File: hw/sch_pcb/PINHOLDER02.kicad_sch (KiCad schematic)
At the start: 5 parts, among them J1 HEADER_1x03, M3 HOLE, M4 HOLE

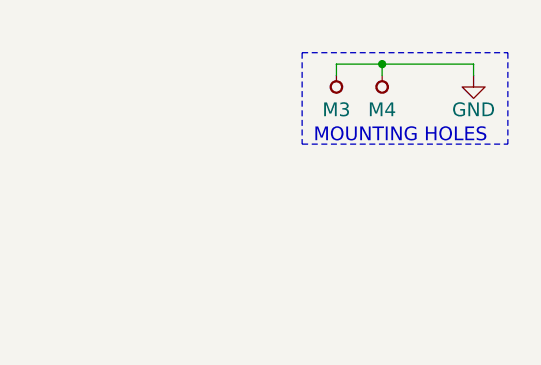
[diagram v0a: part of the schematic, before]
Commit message: uprava layoutu pro PCRD01A
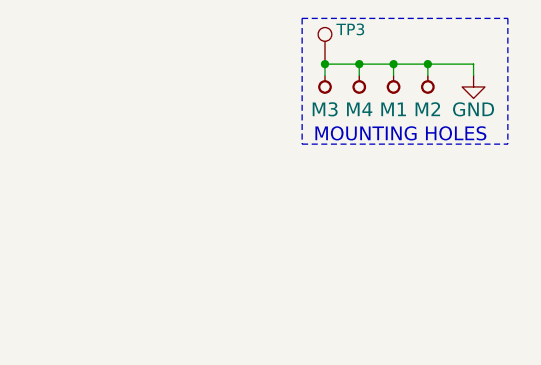
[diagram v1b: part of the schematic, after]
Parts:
- added M1, M2: HOLE, Mlab_Mechanical:MountingHole_3mm, symbol MLAB_MECHANICAL:HOLE
- added TP3: TestPoint, Mlab_CON:TestPoint_Pad_D0.5mm_noSilk, symbol Connector:TestPoint
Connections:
- net GND: now also M1.1, M2.1, TP3.1
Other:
- title: PINHOLDER01A -> PINHOLDER02A
- moved on the sheet: M3, M4
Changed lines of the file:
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@@
   (paper "A4")
   (title_block
-    (title "PINHOLDER01A")
+    (title "PINHOLDER02A")
     (date "2023-04-12")
-    (rev "01A")
+    (rev "02A")
     (company "www.mlab.cz")
   )
-  (junction (at 262.89 22.86) (diameter 0) (color 0 0 0 0)
-  )
-  (wire (pts (xy 262.89 24.13) (xy 262.89 22.86))
+  (junction (at 264.16 22.86) (diameter 0) (color 0 0 0 0)
+  )
+  (junction (at 267.97 22.86) (diameter 0) (color 0 0 0 0)
+  )
+  (junction (at 260.35 22.86) (diameter 0) (color 0 0 0 0)
+  )
+  (junction (at 256.54 22.86) (diameter 0) (color 0 0 0 0)
+  )
+  (wire (pts (xy 267.97 22.86) (xy 267.97 24.13))
+    (stroke (width 0) (type default) (color 0 0 0 0))
+  )
+  (wire (pts (xy 260.35 24.13) (xy 260.35 22.86))
+    (stroke (width 0) (type solid) (color 0 0 0 0))
+  )
+  (wire (pts (xy 260.35 22.86) (xy 264.16 22.86))
     (stroke (width 0) (type solid) (color 0 0 0 0))
   )
@@
     (stroke (width 0) (type default) (color 0 0 0 0))
   )
-  (wire (pts (xy 262.89 22.86) (xy 273.05 22.86))
-    (stroke (width 0) (type solid) (color 0 0 0 0))
-  )
   (wire (pts (xy 116.84 101.6) (xy 146.05 101.6))
     (stroke (width 0) (type default) (color 0 0 0 0))
@@
     (stroke (width 0) (type dash) (color 0 0 0 0))
   )
-  (polyline (pts (xy 254 21.59) (xy 276.86 21.59))
+  (polyline (pts (xy 254 17.78) (xy 276.86 17.78))
     (stroke (width 0) (type dash) (color 0 0 0 0))
   )
@@
     (stroke (width 0) (type default) (color 0 0 0 0))
   )
-  (polyline (pts (xy 276.86 21.59) (xy 276.86 31.75))
+  (polyline (pts (xy 276.86 17.78) (xy 276.86 31.75))
     (stroke (width 0) (type dash) (color 0 0 0 0))
   )
@@
     (stroke (width 0) (type default) (color 0 0 0 0))
   )
-  (wire (pts (xy 257.81 24.13) (xy 257.81 22.86))
-    (stroke (width 0) (type solid) (color 0 0 0 0))
-  )
-  (wire (pts (xy 257.81 22.86) (xy 262.89 22.86))
-    (stroke (width 0) (type solid) (color 0 0 0 0))
-  )
-  (polyline (pts (xy 254 21.59) (xy 254 31.75))
-    (stroke (width 0) (type dash) (color 0 0 0 0))
+  (wire (pts (xy 264.16 22.86) (xy 264.16 24.13))
+    (stroke (width 0) (type default) (color 0 0 0 0))
+  )
+  (wire (pts (xy 264.16 22.86) (xy 267.97 22.86))
+    (stroke (width 0) (type solid) (color 0 0 0 0))
+  )
+  (wire (pts (xy 256.54 24.13) (xy 256.54 22.86))
+    (stroke (width 0) (type solid) (color 0 0 0 0))
+  )
+  (wire (pts (xy 256.54 22.86) (xy 260.35 22.86))
+    (stroke (width 0) (type solid) (color 0 0 0 0))
+  )
+  (polyline (pts (xy 254 17.78) (xy 254 31.75))
+    (stroke (width 0) (type dash) (color 0 0 0 0))
+  )
+  (wire (pts (xy 267.97 22.86) (xy 273.05 22.86))
+    (stroke (width 0) (type solid) (color 0 0 0 0))
   )
   (text "MOUNTING HOLES" (at 255.27 31.75 0)
@@
     (pin "1")
   )
-  (symbol (lib_id "MLAB_MECHANICAL:HOLE") (at 257.81 25.4 90) (unit 1)
-    (in_bom yes) (on_board yes)
-    (property "Reference" "M3" (id 0) (at 257.81 27.94 90)
-      (effects (font (size 1.524 1.524)))
-    )
-    (property "Value" "HOLE" (id 1) (at 260.35 25.4 0)
-      (effects (font (size 1.524 1.524)) hide)
-    )
-    (property "Footprint" "Mlab_Mechanical:MountingHole_3mm" (id 2) (at 257.81 25.4 0)
-      (effects (font (size 1.524 1.524)) hide)
-    )
-    (property "Datasheet" "" (id 3) (at 257.81 25.4 0)
-      (effects (font (size 1.524 1.524)))
+  (symbol (lib_id "MLAB_MECHANICAL:HOLE") (at 264.16 25.4 90) (unit 1)
+    (in_bom yes) (on_board yes)
+    (property "Reference" "M1" (id 0) (at 264.16 27.94 90)
+      (effects (font (size 1.524 1.524)))
+    )
+    (property "Value" "HOLE" (id 1) (at 266.7 25.4 0)
+      (effects (font (size 1.524 1.524)) hide)
+    )
+    (property "Footprint" "Mlab_Mechanical:MountingHole_3mm" (id 2) (at 264.16 25.4 0)
+      (effects (font (size 1.524 1.524)) hide)
+    )
+    (property "Datasheet" "" (id 3) (at 264.16 25.4 0)
+      (effects (font (size 1.524 1.524)))
+    )
+    (pin "1")
+  )
+  (symbol (lib_id "MLAB_MECHANICAL:HOLE") (at 256.54 25.4 90) (unit 1)
+    (in_bom yes) (on_board yes)
+    (property "Reference" "M3" (id 0) (at 256.54 27.94 90)
+      (effects (font (size 1.524 1.524)))
+    )
+    (property "Value" "HOLE" (id 1) (at 259.08 25.4 0)
+      (effects (font (size 1.524 1.524)) hide)
+    )
+    (property "Footprint" "Mlab_Mechanical:MountingHole_3mm" (id 2) (at 256.54 25.4 0)
+      (effects (font (size 1.524 1.524)) hide)
+    )
+    (property "Datasheet" "" (id 3) (at 256.54 25.4 0)
+      (effects (font (size 1.524 1.524)))
+    )
+    (pin "1")
+  )
+  (symbol (lib_id "MLAB_MECHANICAL:HOLE") (at 267.97 25.4 90) (unit 1)
+    (in_bom yes) (on_board yes)
+    (property "Reference" "M2" (id 0) (at 267.97 27.94 90)
+      (effects (font (size 1.524 1.524)))
+    )
+    (property "Value" "HOLE" (id 1) (at 270.51 25.4 0)
+      (effects (font (size 1.524 1.524)) hide)
+    )
+    (property "Footprint" "Mlab_Mechanical:MountingHole_3mm" (id 2) (at 267.97 25.4 0)
+      (effects (font (size 1.524 1.524)) hide)
+    )
+    (property "Datasheet" "" (id 3) (at 267.97 25.4 0)
+      (effects (font (size 1.524 1.524)))
+    )
+    (pin "1")
+  )
+  (symbol (lib_id "Connector:TestPoint") (at 256.54 22.86 0) (unit 1)
+    (in_bom yes) (on_board yes)
+    (property "Reference" "TP3" (id 0) (at 257.81 19.05 0)
+      (effects (font (size 1.27 1.27)) (justify left))
+    )
+    (property "Value" "TestPoint" (id 1) (at 259.08 20.8279 0)
+      (effects (font (size 1.27 1.27)) (justify left) hide)
+    )
+    (property "Footprint" "TestPoint:TestPoint_Pad_D2.0mm" (id 2) (at 261.62 22.86 0)
+      (effects (font (size 1.27 1.27)) hide)
+    )
+    (property "Datasheet" "~" (id 3) (at 261.62 22.86 0)
+      (effects (font (size 1.27 1.27)) hide)
+    )
+    (property "Datasheet" "~" (id 4) (at 256.54 22.86 0)
+      (effects (font (size 1.27 1.27)) hide)
+    )
+    (property "Footprint" "Mlab_CON:TestPoint_Pad_D0.5mm_noSilk" (id 5) (at 256.54 22.86 0)
+      (effects (font (size 1.27 1.27)) hide)
+    )
+    (property "Value" "TestPoint" (id 6) (at 256.54 22.86 0)
+      (effects (font (size 1.27 1.27)) hide)
     )
     (pin "1")
@@
     (pin "1")
   )
-  (symbol (lib_id "MLAB_MECHANICAL:HOLE") (at 262.89 25.4 90) (unit 1)
-    (in_bom yes) (on_board yes)
-    (property "Reference" "M4" (id 0) (at 262.89 27.94 90)
-      (effects (font (size 1.524 1.524)))
-    )
-    (property "Value" "HOLE" (id 1) (at 265.43 25.4 0)
-      (effects (font (size 1.524 1.524)) hide)
-    )
-    (property "Footprint" "Mlab_Mechanical:MountingHole_3mm" (id 2) (at 262.89 25.4 0)
-      (effects (font (size 1.524 1.524)) hide)
-    )
-    (property "Datasheet" "" (id 3) (at 262.89 25.4 0)
+  (symbol (lib_id "MLAB_MECHANICAL:HOLE") (at 260.35 25.4 90) (unit 1)
+    (in_bom yes) (on_board yes)
+    (property "Reference" "M4" (id 0) (at 260.35 27.94 90)
+      (effects (font (size 1.524 1.524)))
+    )
+    (property "Value" "HOLE" (id 1) (at 262.89 25.4 0)
+      (effects (font (size 1.524 1.524)) hide)
+    )
+    (property "Footprint" "Mlab_Mechanical:MountingHole_3mm" (id 2) (at 260.35 25.4 0)
+      (effects (font (size 1.524 1.524)) hide)
+    )
+    (property "Datasheet" "" (id 3) (at 260.35 25.4 0)
       (effects (font (size 1.524 1.524)))
     )
@@
       (reference "J1") (unit 1) (value "HEADER_1x03") (footprint "Connector_PinHeader_2.54mm:PinHeader_1x03_P2.54mm_Vertical_SMD_Pin1Left")
     )
+    (path "/2966c4ec-ab86-48c7-b622-e8ba9ff43a81"
+      (reference "M1") (unit 1) (value "HOLE") (footprint "Mlab_Mechanical:MountingHole_3mm")
+    )
+    (path "/471731a9-774a-4a26-8f31-d71830da0f1d"
+      (reference "M2") (unit 1) (value "HOLE") (footprint "Mlab_Mechanical:MountingHole_3mm")
+    )
     (path "/38b35dd8-1022-49ff-9859-753b58dd2e59"
       (reference "M3") (unit 1) (value "HOLE") (footprint "Mlab_Mechanical:MountingHole_3mm")
@@
       (reference "TP2") (unit 1) (value "TestPoint") (footprint "TestPoint:TestPoint_Keystone_5019_Minature")
     )
-  )
+    (path "/59ab6160-e4b3-4344-a2cb-0c8d55864332"
+      (reference "TP3") (unit 1) (value "TestPoint") (footprint "TestPoint:TestPoint_Pad_D2.0mm")
+    )
+  )
